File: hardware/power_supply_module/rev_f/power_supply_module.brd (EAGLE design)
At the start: 68.1 x 66 mm, 173 parts, among them J1 MODULE_POWER, J3 TC2030-FTDI-I2C, Q1 MOSFET-NCHANNELSMD, U1 TLV62130, U10 LTC2943, U11 LTC2943, U12 LTC2943, U13 LTC2943, U14 LTC2943, U15 LTC2943, U16 LT3652, U17 LM234, U18 MAX17205, U19 ESDR0502N, U2 TLV62130, U20 AP22814, U21 AP22814, U22 AP22814, U23 AP22814, U24 AP22814, U25 PCA9544AQFN-N20, U26 LTC2943, U27 MAX6746, U28 3.3V, U29 M24C01WMN, U3 TLV62130, U30 SN74AUP1T14DCKR, U4 TLV62130, U5 TLV62130, U6 PCA9544AQFN-N20, U7 PCA9544AQFN-N20, U8 LTC2941, U9 LTC2943

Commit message: Ran the script, generate gerbers
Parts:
- added !RESET: TEST_POINT_0.040IN, headers:TESTPOINT_0.040IN
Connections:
- removed net ENABLE: U1.13, U2.13, U27.7, U3.13, U30.2, U4.13, U5.13
- new net !RESET: !RESET.TESTPOINT, U1.13, U2.13, U27.7, U3.13, U30.2, U4.13, U5.13
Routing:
- net !RESET: track 0.00 -> 95.3 mm, vias 0 -> 6
- net ENABLE: track 88.4 -> 0.00 mm, vias 6 -> 0
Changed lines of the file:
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@@
 <element name="R70" library="passives" package="0402_RES" value="150 Ω" x="18.034" y="35.306" smashed="yes" rot="R90">
 <attribute name="DIGIKEY" value="P150LCT-ND" x="18.034" y="35.306" size="1.778" layer="27" rot="R90" display="off"/>
-<attribute name="NAME" x="17.272" y="36.322" size="1.016" layer="25" font="vector" ratio="12" align="bottom-center"/>
+<attribute name="NAME" x="17.526" y="36.576" size="1.016" layer="25" font="vector" ratio="12" rot="R90" align="bottom-center"/>
 <attribute name="VALUE" x="19.431" y="35.306" size="1.016" layer="27" font="vector" ratio="12" rot="R90" align="bottom-center"/>
 </element>
@@
 <attribute name="NAME" x="23.241" y="36.83" size="1.016" layer="25" font="vector" ratio="12" rot="R270" align="bottom-center"/>
 <attribute name="VALUE" x="21.209" y="36.576" size="1.016" layer="27" font="vector" ratio="12" rot="R270" align="bottom-center"/>
+</element>
+<element name="!RESET" library="headers" package="TESTPOINT_0.040IN" value="TEST_POINT_0.040IN" x="14.732" y="38.608">
+<attribute name="DIGIKEY" value="5001K-ND" x="14.732" y="38.608" size="1.778" layer="27" display="off"/>
 </element>
 </elements>
@@
 <via x="65.913" y="33.147" extent="1-16" drill="0.254"/>
 <via x="65.913" y="24.003" extent="1-16" drill="0.254"/>
-<via x="15.113" y="39.497" extent="1-16" drill="0.254"/>
+<via x="18.034" y="40.132" extent="1-16" drill="0.254"/>
 <via x="27.178" y="47.244" extent="1-16" drill="0.254"/>
 <via x="26.67" y="44.45" extent="1-16" drill="0.254"/>
@@
 </polygon>
 </signal>
-<signal name="ENABLE">
+<signal name="N$77">
+<contactref element="Q1" pad="2"/>
+<contactref element="R66" pad="2"/>
+<wire x1="21.27" y1="35.576" x2="22.03906875" y2="35.576" width="0.254" layer="1"/>
+<wire x1="22.03906875" y1="35.576" x2="22.606" y2="36.14293125" width="0.254" layer="1"/>
+</signal>
+<signal name="N$40">
+<contactref element="R70" pad="2"/>
+<contactref element="Q1" pad="1"/>
+<wire x1="18.034" y1="35.73906875" x2="19.20693125" y2="35.73906875" width="0.254" layer="1"/>
+<wire x1="19.20693125" y1="35.73906875" x2="19.37" y2="35.576" width="0.254" layer="1"/>
+</signal>
+<signal name="N$65">
+<contactref element="R70" pad="1"/>
+<contactref element="U30" pad="4"/>
+<wire x1="18.034" y1="34.87293125" x2="16.89693125" y2="34.87293125" width="0.254" layer="1"/>
+<wire x1="16.89693125" y1="34.87293125" x2="16.398" y2="34.374" width="0.254" layer="1"/>
+</signal>
+<signal name="!RESET">
+<contactref element="!RESET" pad="TESTPOINT"/>
+<contactref element="U27" pad="7"/>
+<contactref element="U30" pad="2"/>
 <contactref element="U2" pad="13"/>
 <contactref element="U4" pad="13"/>
@@
 <wire x1="13.462" y1="9.652" x2="10.922" y2="12.192" width="0.254" layer="16"/>
 <wire x1="13.462" y1="9.652" x2="16.764" y2="9.652" width="0.254" layer="16"/>
-<contactref element="U27" pad="7"/>
-<contactref element="U30" pad="2"/>
-<wire x1="15.748" y1="32.174" x2="15.748" y2="31.496" width="0.254" layer="1"/>
-<wire x1="15.748" y1="31.496" x2="15.494" y2="31.242" width="0.254" layer="1"/>
+<wire x1="15.494" y1="31.242" x2="15.748" y2="31.496" width="0.254" layer="1"/>
 <wire x1="15.494" y1="31.242" x2="12.7" y2="31.242" width="0.254" layer="1"/>
 <wire x1="12.7" y1="31.242" x2="11.43" y2="32.512" width="0.254" layer="1"/>
-<wire x1="11.43" y1="32.512" x2="10.385" y2="32.512" width="0.254" layer="1"/>
-<wire x1="10.385" y1="32.512" x2="10.314" y2="32.583" width="0.254" layer="1"/>
 <wire x1="10.922" y1="29.464" x2="12.7" y2="31.242" width="0.254" layer="16"/>
 <wire x1="10.922" y1="12.192" x2="10.922" y2="29.464" width="0.254" layer="16"/>
 <via x="12.7" y="31.242" extent="1-16" drill="0.254"/>
-</signal>
-<signal name="N$77">
-<contactref element="Q1" pad="2"/>
-<contactref element="R66" pad="2"/>
-<wire x1="21.27" y1="35.576" x2="22.03906875" y2="35.576" width="0.254" layer="1"/>
-<wire x1="22.03906875" y1="35.576" x2="22.606" y2="36.14293125" width="0.254" layer="1"/>
-</signal>
-<signal name="N$40">
-<contactref element="R70" pad="2"/>
-<contactref element="Q1" pad="1"/>
-<wire x1="18.034" y1="35.73906875" x2="19.20693125" y2="35.73906875" width="0.254" layer="1"/>
-<wire x1="19.20693125" y1="35.73906875" x2="19.37" y2="35.576" width="0.254" layer="1"/>
-</signal>
-<signal name="N$65">
-<contactref element="R70" pad="1"/>
-<contactref element="U30" pad="4"/>
-<wire x1="18.034" y1="34.87293125" x2="16.89693125" y2="34.87293125" width="0.254" layer="1"/>
-<wire x1="16.89693125" y1="34.87293125" x2="16.398" y2="34.374" width="0.254" layer="1"/>
+<wire x1="15.748" y1="31.496" x2="15.748" y2="32.174" width="0.254" layer="1"/>
+<wire x1="15.748" y1="32.174" x2="15.748" y2="37.592" width="0.254" layer="1"/>
+<wire x1="15.748" y1="37.592" x2="14.732" y2="38.608" width="0.254" layer="1"/>
+<wire x1="11.43" y1="32.512" x2="10.385" y2="32.512" width="0.254" layer="1"/>
+<wire x1="10.385" y1="32.512" x2="10.314" y2="32.583" width="0.254" layer="1"/>
 </signal>
 </signals>

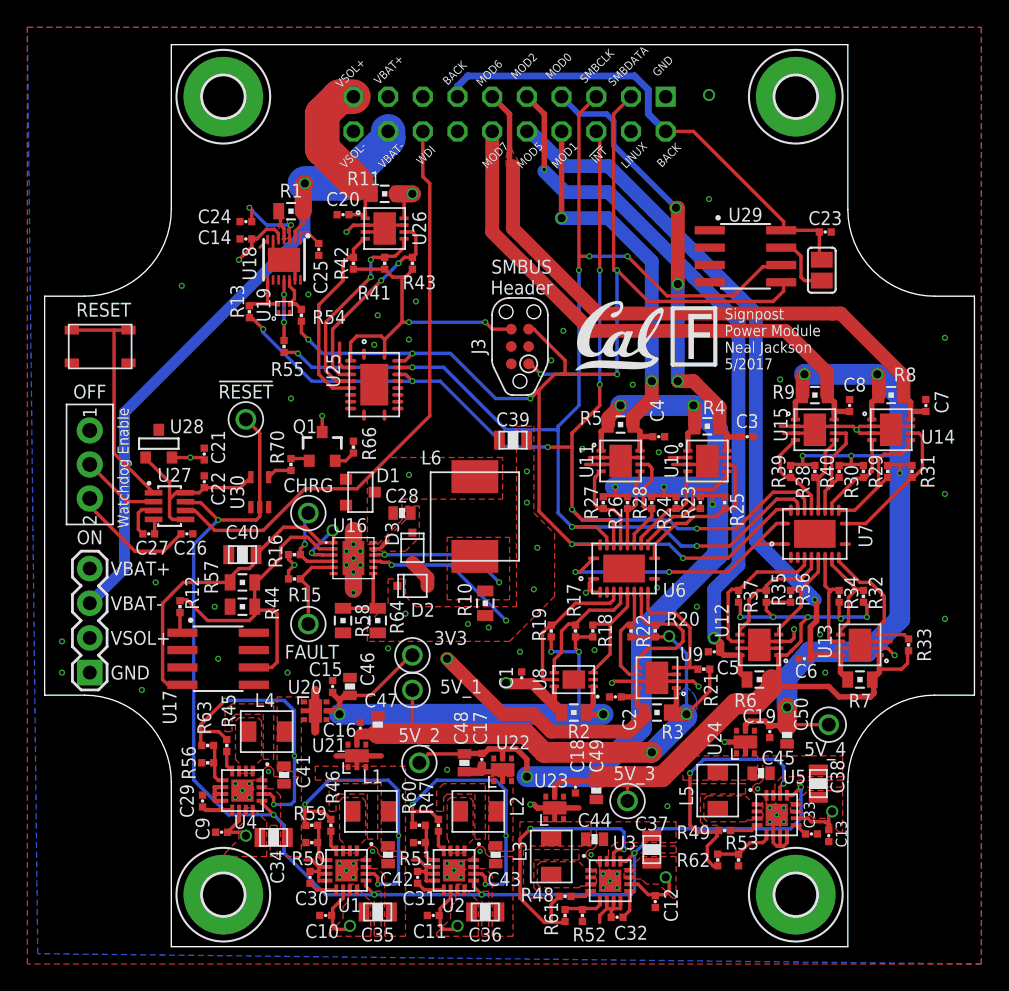
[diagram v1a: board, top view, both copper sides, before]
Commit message: Fix up component names
Change gnd symbol to SUPPLY, test points to TP, and switches to S. Works
better with eagle bom script
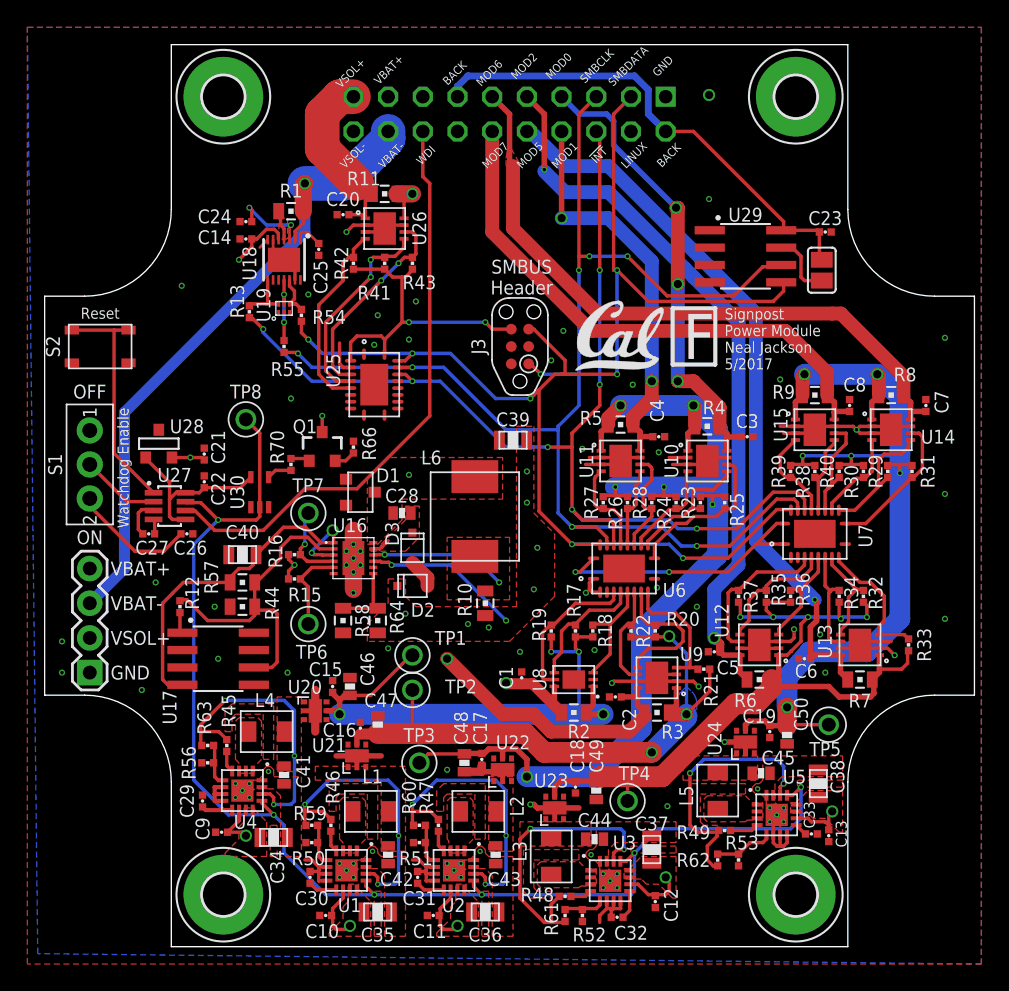
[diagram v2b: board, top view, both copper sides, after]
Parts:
- D2: value (none) -> DIODE_ZENERSOT323
- D3: value DIODE_SCHOTTKYSOD323 -> None
- renumbered !RESET to TP8, 3V3 to TP1, 5V_1 to TP2, 5V_2 to TP3, 5V_3 to TP4, 5V_4 to TP5, CHRG to TP7, FAULT to TP6, RESET to S2
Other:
- board text added: "Reset"

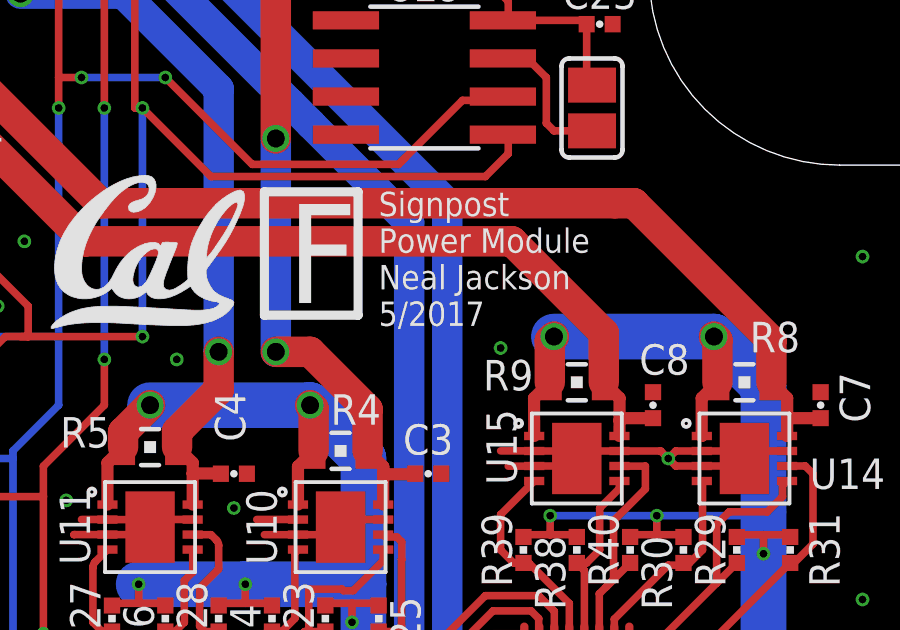
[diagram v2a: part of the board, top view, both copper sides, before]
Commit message: add manufacturer pns
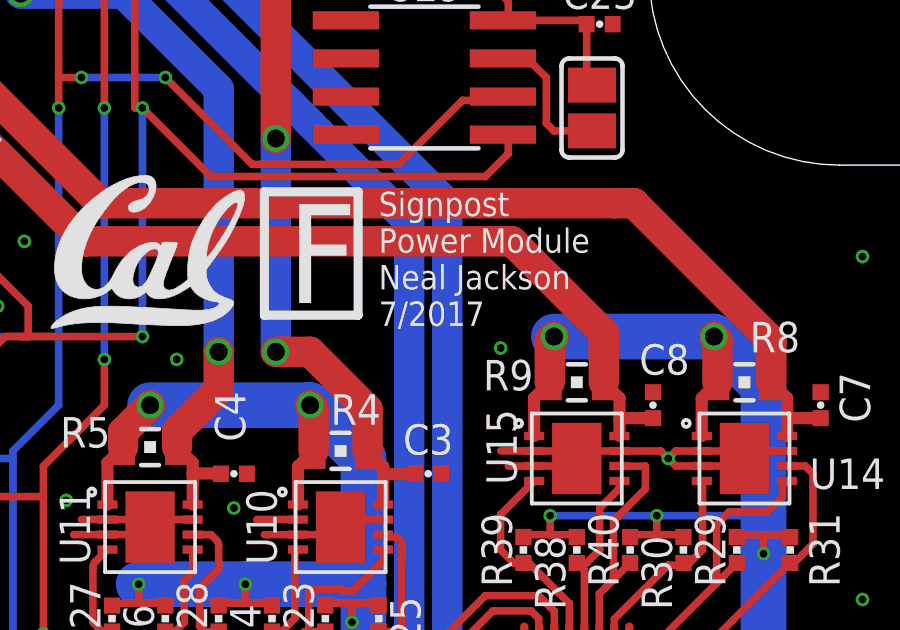
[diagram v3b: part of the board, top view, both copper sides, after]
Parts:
- D3: value None -> (none)
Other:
- board text added: "Signpost Power Module Neal Jackson 7/2017"
- board text removed: "Signpost Power Module Neal Jackson 5/2017"
